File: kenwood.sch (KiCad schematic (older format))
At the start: 18 parts, among them IC1 ATMEGA168-A, P6 CONN_1, P7 CONN_1, P8 CONN_1, U2 DMP2066LSD, U4 MC33064D, U7 TSOP382

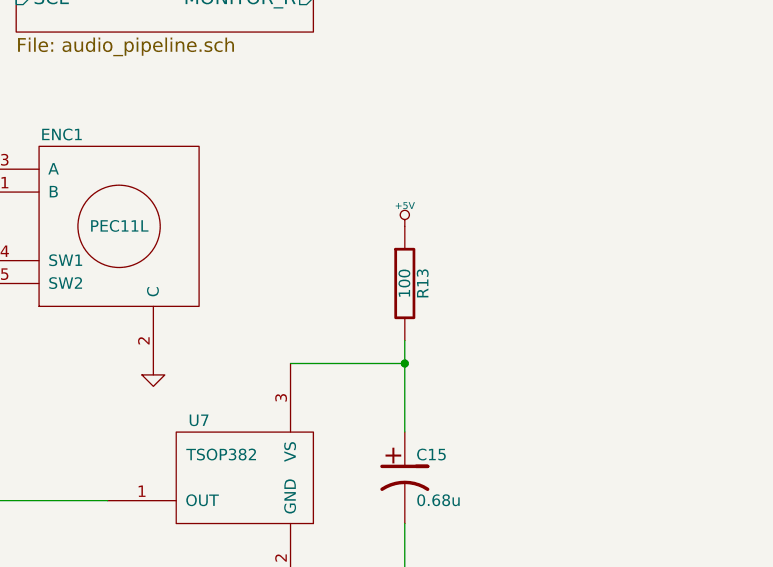
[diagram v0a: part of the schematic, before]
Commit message: Adding part numbers for everything, for BOM preparation.
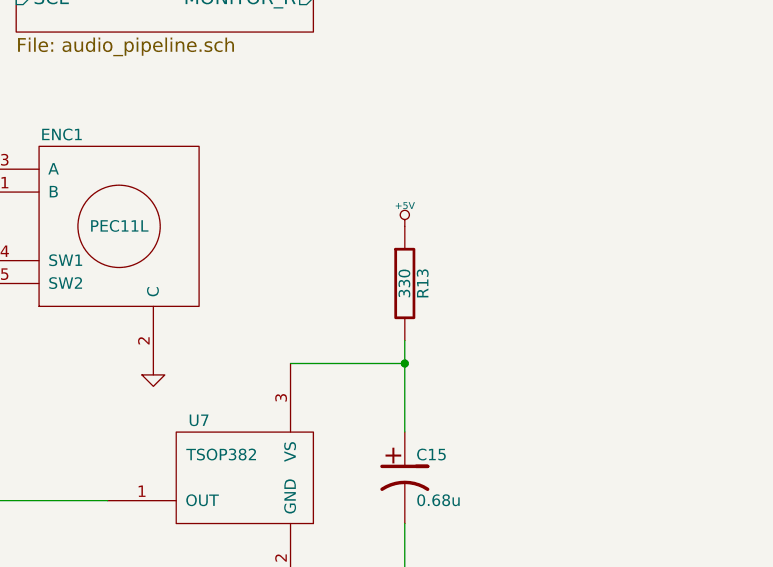
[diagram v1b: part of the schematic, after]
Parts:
- C15, C5: Digikey (none) -> 490-1541-1-ND
- C3: Digikey (none) -> 445-5122-1-ND
- D1: Digikey (none) -> 475-2558-1-ND
- ENC1: DNP (none) -> 1; Digikey (none) -> -; Mouser (none) -> 652-PEC11-4220K-S24
- IC1: Digikey (none) -> ATMEGA168A-AU-ND
- ICSP1: Digikey (none) -> 609-3218-ND
- LDD1: Digikey (none) -> 67-1470-ND
- R13: value 100 -> 330; Digikey (none) -> P330GCT-ND
- R5: Digikey (none) -> P330GCT-ND
- SERIAL1: Digikey (none) -> 609-3263-ND
- U2: Digikey (none) -> DMP2066LSDDICT-ND
- U4: DNP (none) -> 1; Digikey (none) -> MC33064D-5GOS-ND
- U7: Digikey (none) -> 751-1227-ND
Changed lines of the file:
@@
-EESchema Schematic File Version 2  date 8/3/2012 1:01:40 PM
+EESchema Schematic File Version 2  date 8/3/2012 4:17:04 PM
 LIBS:atmel
 LIBS:device
@@
 F 0 "U4" H 2400 4700 50  0000 C CNN
 F 1 "MC33064D" H 2650 4304 50  0000 C CNN
+F 4 "MC33064D-5GOS-ND" H 2350 4500 60  0001 C CNN "Digikey"
+F 5 "1" H 2350 4500 60  0001 C CNN "DNP"
 	1    2350 4500
 	1    0    0    -1
@@
 F 0 "R5" V 6580 5600 50  0000 C CNN
 F 1 "330" V 6500 5600 50  0000 C CNN
+F 4 "P330GCT-ND" H 6500 5600 60  0001 C CNN "Digikey"
 	1    6500 5600
 	1    0    0    -1
@@
 F 0 "D1" H 6500 5250 50  0000 C CNN
 F 1 "LED" H 6500 5050 50  0000 C CNN
+F 4 "475-2558-1-ND" H 6500 5150 60  0001 C CNN "Digikey"
 	1    6500 5150
 	0    1    1    0
@@
 F 1 "ATMEGA168-A" H 5250 1900 50  0000 L BNN
 F 2 "TQFP32" H 4450 1950 50  0001 C CNN
+F 4 "ATMEGA168A-AU-ND" H 5000 3300 60  0001 C CNN "Digikey"
 	1    5000 3300
 	1    0    0    -1
@@
 F 0 "C5" H 3750 2500 50  0000 L CNN
 F 1 "0.68u" H 3750 2300 50  0000 L CNN
+F 4 "490-1541-1-ND" H 3700 2400 60  0001 C CNN "Digikey"
 	1    3700 2400
 	1    0    0    -1
@@
 F 2 "MODULE" H 9900 1600 50  0001 C CNN
 F 3 "DOCUMENTATION" H 9900 1600 50  0001 C CNN
+F 4 "DMP2066LSDDICT-ND" H 9900 1600 60  0001 C CNN "Digikey"
 	1    9900 1600
 	-1   0    0    -1
@@
 F 0 "C15" H 9500 5950 50  0000 L CNN
 F 1 "0.68u" H 9500 5750 50  0000 L CNN
+F 4 "490-1541-1-ND" H 9450 5850 60  0001 C CNN "Digikey"
 	1    9450 5850
 	1    0    0    -1
@@
 P 9450 5000
 F 0 "R13" V 9530 5000 50  0000 C CNN
-F 1 "100" V 9450 5000 50  0000 C CNN
+F 1 "330" V 9450 5000 50  0000 C CNN
+F 4 "P330GCT-ND" H 9450 5000 60  0001 C CNN "Digikey"
 	1    9450 5000
 	1    0    0    -1
@@
 F 1 "TSOP382" H 8650 5950 50  0000 C CNN
 F 2 "SIP3" H 8550 5600 50  0001 C CNN
+F 4 "751-1227-ND" H 8800 5850 60  0001 C CNN "Digikey"
 	1    8800 5850
 	1    0    0    -1
@@
 F 1 "PEC11L" H 8200 4750 50  0000 C CNN
 F 2 "MODULE" H 8000 4400 50  0001 C CNN
+F 4 "-" H 8200 4750 60  0001 C CNN "Digikey"
+F 5 "652-PEC11-4220K-S24" H 8200 4750 60  0001 C CNN "Mouser"
+F 6 "1" H 8200 4750 60  0001 C CNN "DNP"
 	1    8200 4750
 	1    0    0    -1
@@
 F 0 "LDD1" H 7900 3000 60  0000 C CNN
 F 1 "LDD-A812RI" H 7900 2000 60  0000 C CNN
+F 4 "67-1470-ND" H 7900 2500 60  0001 C CNN "Digikey"
 	1    7900 2500
 	1    0    0    -1
@@
 F 0 "C3" H 3050 6100 50  0000 L CNN
 F 1 "0.1u" H 3050 5900 50  0000 L CNN
+F 4 "445-5122-1-ND" H 3000 6000 60  0001 C CNN "Digikey"
 	1    3000 6000
 	0    1    1    0
@@
 F 0 "SERIAL1" V 3500 5750 60  0000 C CNN
 F 1 "CONN_6" V 3600 5750 60  0000 C CNN
+F 4 "609-3263-ND" V 3550 5750 60  0001 C CNN "Digikey"
 	1    3550 5750
 	1    0    0    -1
@@
 F 0 "ICSP1" H 5900 1750 50  0000 C CNN
 F 1 "CONN_3X2" V 5900 1550 40  0000 C CNN
+F 4 "609-3218-ND" H 5900 1500 60  0001 C CNN "Digikey"
 	1    5900 1500
 	1    0    0    -1
